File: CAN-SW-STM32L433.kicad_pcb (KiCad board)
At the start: 2 copper layers, 60 x 40 mm, 8 parts, among them U1 STM32L433CCTx

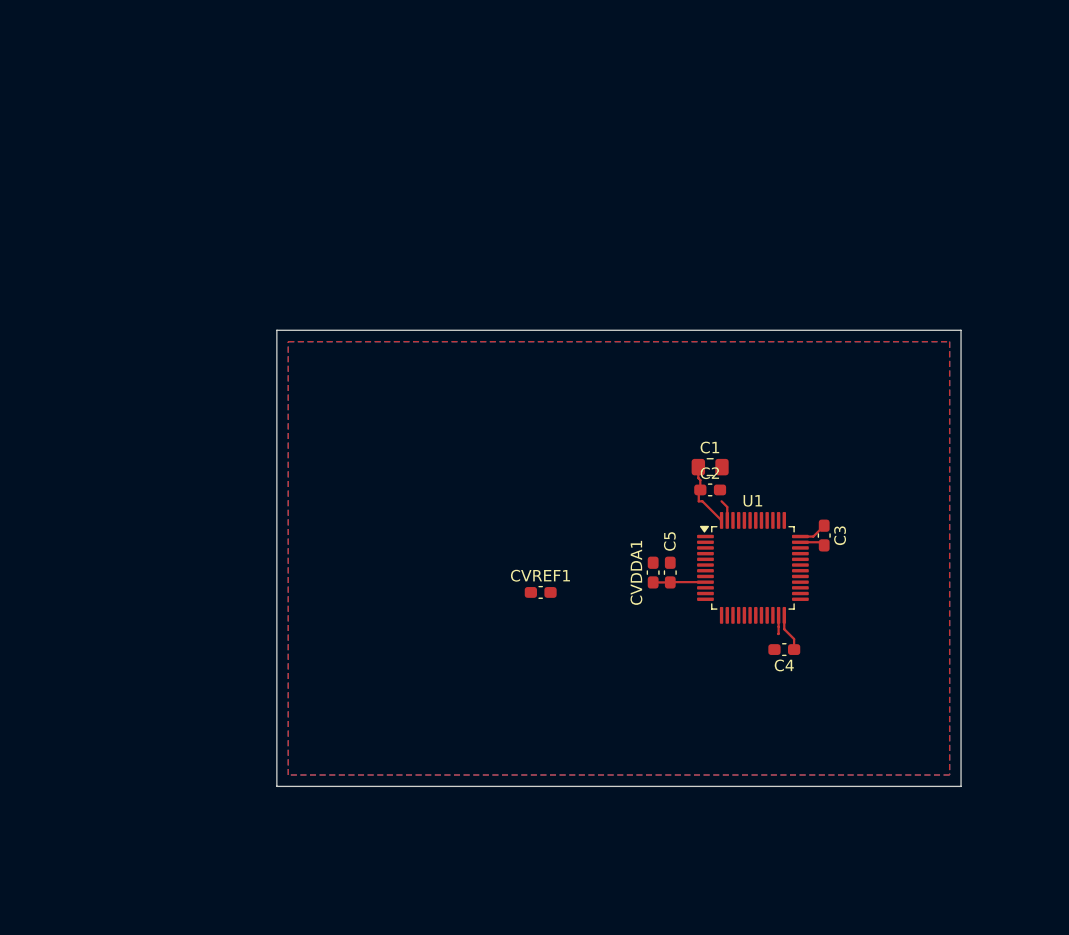
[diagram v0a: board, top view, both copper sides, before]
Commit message: still adding parts, working on basic layout
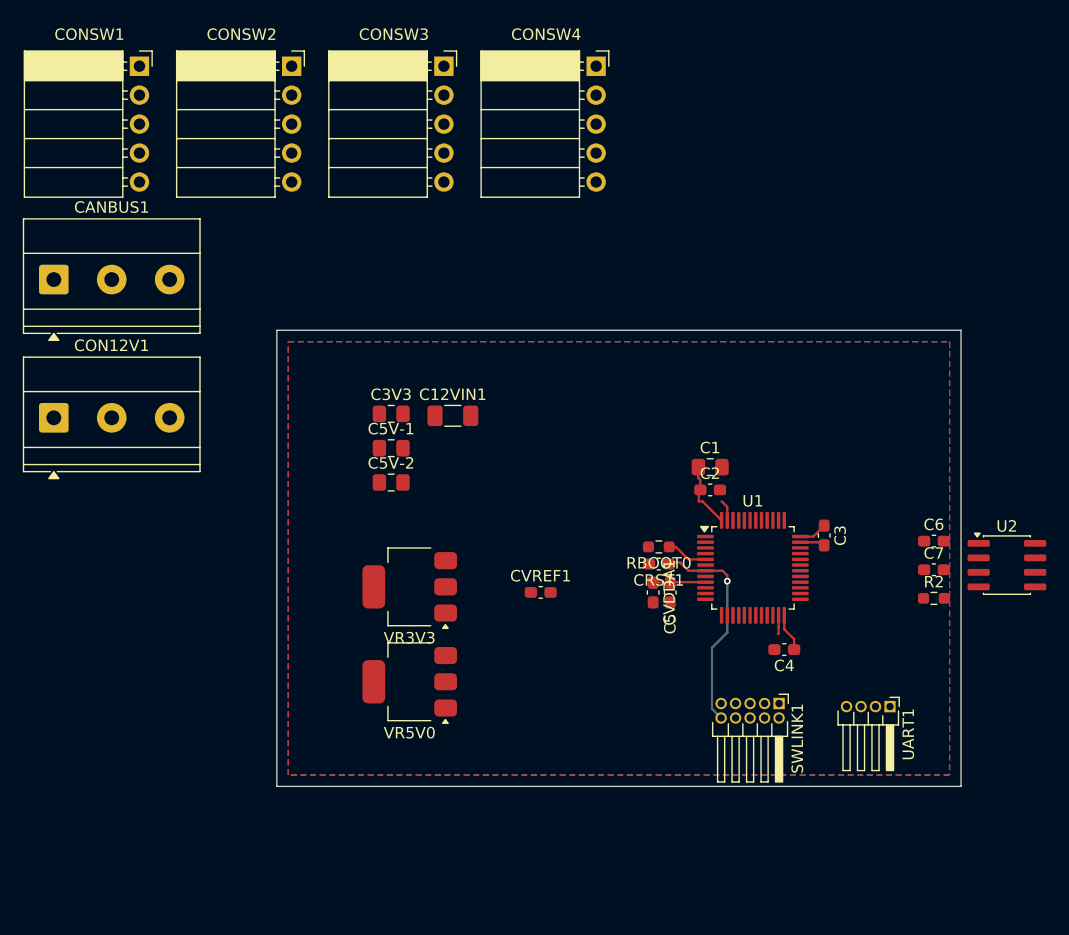
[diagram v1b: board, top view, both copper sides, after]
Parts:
- added C12VIN1: 1u, Capacitor_SMD:C_1206_3216Metric_Pad1.33x1.80mm_HandSolder, F.Cu at (122.4, 85.5)
- added C3V3: 1u, Capacitor_SMD:C_0805_2012Metric_Pad1.18x1.45mm_HandSolder, F.Cu at (117.0, 85.3)
- added C5V-1: 1u, Capacitor_SMD:C_0805_2012Metric_Pad1.18x1.45mm_HandSolder, F.Cu at (117.0, 88.3)
- added C5V-2: 1u, Capacitor_SMD:C_0805_2012Metric_Pad1.18x1.45mm_HandSolder, F.Cu at (117.0, 91.3)
- added C6: 100n, Capacitor_SMD:C_0603_1608Metric_Pad1.08x0.95mm_HandSolder, F.Cu at (164.6, 96.5)
- added C7: 100n, Capacitor_SMD:C_0603_1608Metric_Pad1.08x0.95mm_HandSolder, F.Cu at (164.6, 99.0)
- added CANBUS1: Screw_Terminal_01x03, TerminalBlock_Phoenix:TerminalBlock_Phoenix_MKDS-1,5-3-5.08_1x03_P5.08mm_Horizontal, F.Cu at (87.4, 73.5)
- added CON12V1: CENTER+, TerminalBlock_Phoenix:TerminalBlock_Phoenix_MKDS-1,5-3-5.08_1x03_P5.08mm_Horizontal, F.Cu at (87.4, 85.7)
- added CONSW1: Conn_01x05, Connector_PinSocket_2.54mm:PinSocket_1x05_P2.54mm_Horizontal, F.Cu at (95.0, 54.8)
- added CONSW2: Conn_01x05, Connector_PinSocket_2.54mm:PinSocket_1x05_P2.54mm_Horizontal, F.Cu at (108.3, 54.8)
- added CONSW3: Conn_01x05, Connector_PinSocket_2.54mm:PinSocket_1x05_P2.54mm_Horizontal, F.Cu at (121.7, 54.8)
- added CONSW4: Conn_01x05, Connector_PinSocket_2.54mm:PinSocket_1x05_P2.54mm_Horizontal, F.Cu at (135.0, 54.8)
- added CRST1: 100n, Capacitor_SMD:C_0603_1608Metric_Pad1.08x0.95mm_HandSolder, F.Cu at (140.5, 98.5)
- added R2: 10K, Resistor_SMD:R_0603_1608Metric_Pad0.98x0.95mm_HandSolder, F.Cu at (164.6, 101.5)
- added RBOOT0: 10K, Resistor_SMD:R_0603_1608Metric_Pad0.98x0.95mm_HandSolder, F.Cu at (140.5, 97.0)
- added SWLINK1: Conn_ARM_JTAG_SWD_10, Connector_PinHeader_1.27mm:PinHeader_2x05_P1.27mm_Horizontal, F.Cu at (151.0, 110.7)
- added U2: MCP2562-E-SN, Package_SO:SOIC-8_3.9x4.9mm_P1.27mm, F.Cu at (171.0, 98.6)
- added UART1: Conn_01x04, Connector_PinHeader_1.27mm:PinHeader_1x04_P1.27mm_Horizontal, F.Cu at (160.8, 111.0)
- added VR3V3: TLV1117-33, Package_TO_SOT_SMD:SOT-223-3_TabPin2, F.Cu at (118.7, 100.5)
- added VR5V0: TLV1117-50, Package_TO_SOT_SMD:SOT-223-3_TabPin2, F.Cu at (118.7, 108.8)
- moved C5 1.75 mm to (141.5, 101.0), turned to -90 degrees
- moved CVDDA1 1.75 mm to (140.0, 101.0), turned to -90 degrees
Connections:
- U1 pad 10: unconnected-(U1-PA0-Pad10) -> /ADC1_IN5
- U1 pad 11: unconnected-(U1-PA1-Pad11) -> /ADC1_IN6
- U1 pad 12: unconnected-(U1-PA2-Pad12) -> /ADC1_IN7
- U1 pad 13: unconnected-(U1-PA3-Pad13) -> /ADC1_IN8
- U1 pad 14: unconnected-(U1-PA4-Pad14) -> /ADC1_IN9
- U1 pad 15: unconnected-(U1-PA5-Pad15) -> /ADC1_IN10
- U1 pad 16: unconnected-(U1-PA6-Pad16) -> /ADC1_IN11
- U1 pad 17: unconnected-(U1-PA7-Pad17) -> /ADC1_IN12
- U1 pad 30: unconnected-(U1-PA9-Pad30) -> /USART1_TX
- U1 pad 31: unconnected-(U1-PA10-Pad31) -> /USART1_RX
- U1 pad 34: unconnected-(U1-PA13-Pad34) -> /SWDIO
- U1 pad 37: unconnected-(U1-PA14-Pad37) -> /SWCLK
- U1 pad 39: unconnected-(U1-PB3-Pad39) -> /SWO
- U1 pad 45: unconnected-(U1-PB8-Pad45) -> /CAN1_RX
- U1 pad 46: unconnected-(U1-PB9-Pad46) -> /CAN1_TX
- U1 pad 5: unconnected-(U1-PH0-Pad5) -> /BOOT0
- U1 pad 7: unconnected-(U1-NRST-Pad7) -> /NRST
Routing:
- net /NRST: track 0.00 -> 18.9 mm, vias 0 -> 1
- net /BOOT0: track 0.00 -> 3.63 mm
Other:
- rule pad_to_mask_clearance: 0 -> 0.0508

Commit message: almost done adding parts, working more on layout
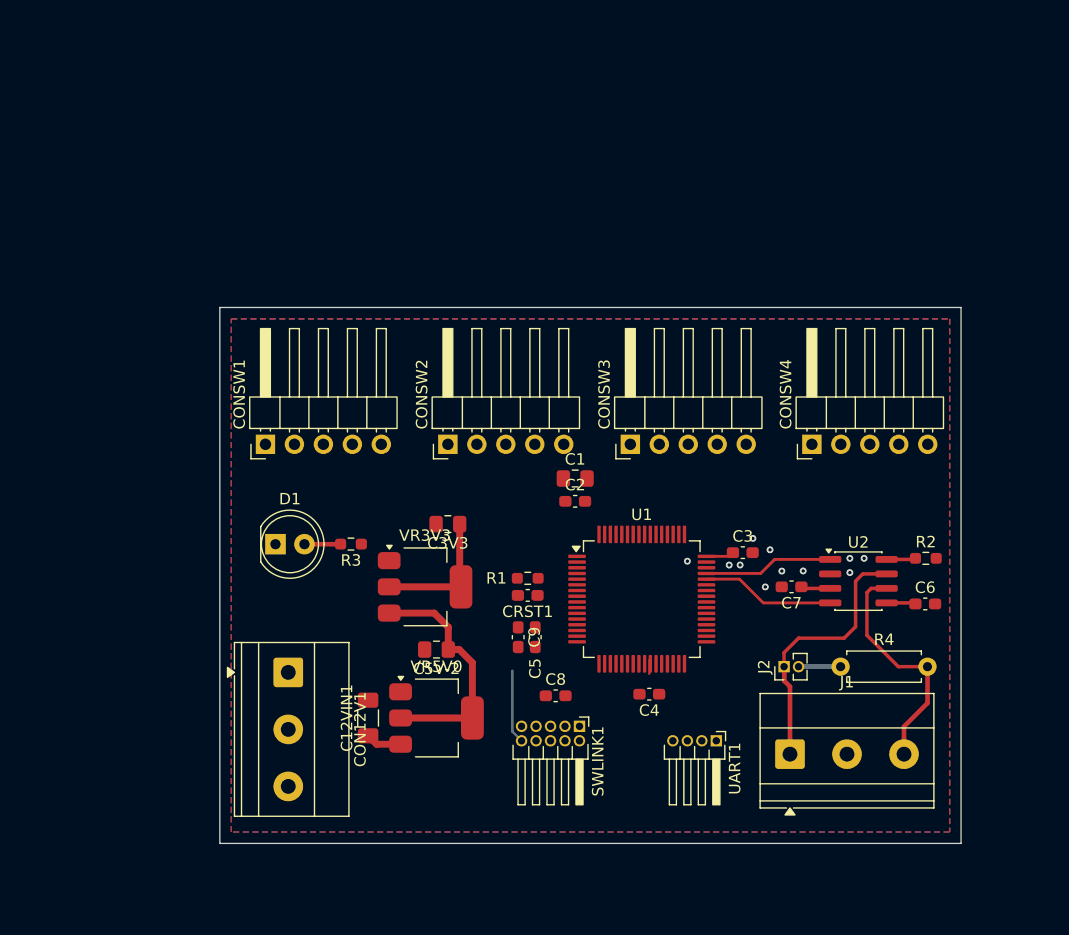
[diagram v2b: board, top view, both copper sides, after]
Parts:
- removed C5V-1: 1u, Capacitor_SMD:C_0805_2012Metric_Pad1.18x1.45mm_HandSolder
- removed CVREF1: 100n, Capacitor_SMD:C_0603_1608Metric_Pad1.08x0.95mm_HandSolder
- added C8: 100n, Capacitor_SMD:C_0603_1608Metric_Pad1.08x0.95mm_HandSolder, F.Cu at (131.4, 110.1)
- added D1: RED, LED_THT:LED_D5.0mm_Clear, F.Cu at (106.9, 96.8)
- added J2: TERM, Connector_PinHeader_1.27mm:PinHeader_1x02_P1.27mm_Vertical, F.Cu at (151.5, 107.5)
- added R3: 1K, Resistor_SMD:R_0603_1608Metric_Pad0.98x0.95mm_HandSolder, F.Cu at (113.5, 96.8)
- added R4: 120R, Resistor_THT:R_Axial_DIN0207_L6.3mm_D2.5mm_P7.62mm_Horizontal, F.Cu at (156.4, 107.5)
- CON12V1: footprint TerminalBlock_Phoenix:TerminalBlock_Phoenix_MKDS-1,5-3-5.08_1x03_P5.08mm_Horizontal -> TerminalBlock_Phoenix:TerminalBlock_Phoenix_MKDS-1,5-3_1x03_P5.00mm_Horizontal
- CONSW1, CONSW2, CONSW3, CONSW4: footprint Connector_PinSocket_2.54mm:PinSocket_1x05_P2.54mm_Horizontal -> Connector_PinHeader_2.54mm:PinHeader_1x05_P2.54mm_Horizontal
- J1: renamed from CANBUS1; value Screw_Terminal_01x03 -> CANBUS; footprint TerminalBlock_Phoenix:TerminalBlock_Phoenix_MKDS-1,5-3-5.08_1x03_P5.08mm_Horizontal -> TerminalBlock_Phoenix:TerminalBlock_Phoenix_MKDS-1,5-3_1x03_P5.00mm_Horizontal
- U1: value STM32L433CCTx -> STM32L433RBTx; footprint Package_QFP:LQFP-48_7x7mm_P0.5mm -> Package_QFP:LQFP-64_10x10mm_P0.5mm
- moved J1 76.8 mm to (152.0, 115.2)
- moved CONSW4 38.2 mm to (153.9, 88.0), turned to 90 degrees
- moved CONSW3 37.0 mm to (138.0, 88.0), turned to 90 degrees
- moved CONSW2 35.9 mm to (122.0, 88.0), turned to 90 degrees
- moved CONSW1 35.0 mm to (106.0, 88.0), turned to 90 degrees
- moved CON12V1 30.3 mm to (108.0, 108.0), turned to -90 degrees
- moved C12VIN1 27.5 mm to (115.0, 112.0), turned to 90 degrees
- moved SWLINK1 17.6 mm to (133.5, 112.7)
- moved UART1 15.5 mm to (145.5, 114.0)
- moved C5V-2 15.2 mm to (121.0, 106.0), turned to 180 degrees
- moved U2 13.1 mm to (158.0, 100.0)
- moved C7 12.6 mm to (152.1, 100.5), turned to 180 degrees
- moved C4 12.5 mm to (139.7, 109.9)
- moved C5 12.5 mm to (129.7, 104.9)
- moved C9 12.5 mm to (128.2, 104.9)
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- renumbered CVDDA1 to C9, RBOOT0 to R1
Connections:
- J1 pad 1: /CANL -> /CANH
- J1 pad 3: /CANH -> /CANL
- U1 pad 10: /ADC1_IN5 -> /ADC1_IN3
- U1 pad 11: /ADC1_IN6 -> /ADC1_IN4
- U1 pad 12: /ADC1_IN7 -> GND
- U1 pad 13: /ADC1_IN8 -> +3.3V
- U1 pad 14: /ADC1_IN9 -> /ADC1_IN5
- U1 pad 15: /ADC1_IN10 -> /ADC1_IN6
- U1 pad 16: /ADC1_IN11 -> /ADC1_IN7
- U1 pad 17: /ADC1_IN12 -> /ADC1_IN8
- U1 pad 18: unconnected-(U1-PB0-Pad18) -> GND
- U1 pad 19: unconnected-(U1-PB1-Pad19) -> +3.3V
- U1 pad 20: unconnected-(U1-PB2-Pad20) -> /ADC1_IN9
- U1 pad 21: unconnected-(U1-PB10-Pad21) -> /ADC1_IN10
- U1 pad 22: unconnected-(U1-PB11-Pad22) -> /ADC1_IN11
- U1 pad 23: GND -> /ADC1_IN12
- U1 pad 24: +3.3V -> unconnected-(U1-PC4-Pad24)
- U1 pad 30: /USART1_TX -> unconnected-(U1-PB11-Pad30)
- U1 pad 31: /USART1_RX -> GND
- U1 pad 32: unconnected-(U1-PA11-Pad32) -> +3.3V
- U1 pad 34: /SWDIO -> unconnected-(U1-PB13-Pad34)
- U1 pad 35: GND -> unconnected-(U1-PB14-Pad35)
- U1 pad 36: +3.3V -> unconnected-(U1-PB15-Pad36)
- U1 pad 37: /SWCLK -> unconnected-(U1-PC6-Pad37)
- U1 pad 39: /SWO -> unconnected-(U1-PC8-Pad39)
- U1 pad 42: unconnected-(U1-PB6-Pad42) -> /USART1_TX
- U1 pad 43: unconnected-(U1-PB7-Pad43) -> /USART1_RX
- U1 pad 44: unconnected-(U1-PH3-Pad44) -> /CAN1_RX
- U1 pad 45: /CAN1_RX -> /CAN1_TX
- U1 pad 46: /CAN1_TX -> /SWDIO
- U1 pad 8: GND -> /ADC1_IN1
- U1 pad 9: +3.3V -> /ADC1_IN2
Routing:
- net +5V: track 0.00 -> 24.0 mm
- net /CANH: track 0.00 -> 23.3 mm
- net /CANL: track 0.00 -> 20.6 mm
- net /NRST: track 18.9 -> 6.49 mm, vias 1 -> 0
- net /CAN1_RX: track 0.00 -> 11.7 mm
- net /CAN1_TX: track 0.00 -> 11.4 mm
- net GND: track 5.74 -> 0.00 mm, vias 0 -> 11
- net Net-(J2-Pin_2): track 0.00 -> 3.69 mm
- net /BOOT0: track 3.63 -> 0.00 mm
- net Net-(D1-A): track 0.00 -> 3.17 mm
- net +12V: track 0.00 -> 3.16 mm
- net Net-(U2-STBY): track 0.00 -> 2.56 mm
- net unconnected-(U1-PB0-Pad26): track 0.00 -> 1.22 mm
- net +3.3V: track 16.3 -> 16.8 mm
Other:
- board size 60 x 40 mm -> 65 x 47 mm

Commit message: more progress on the layout, fixed connector sizes for uart and swlink
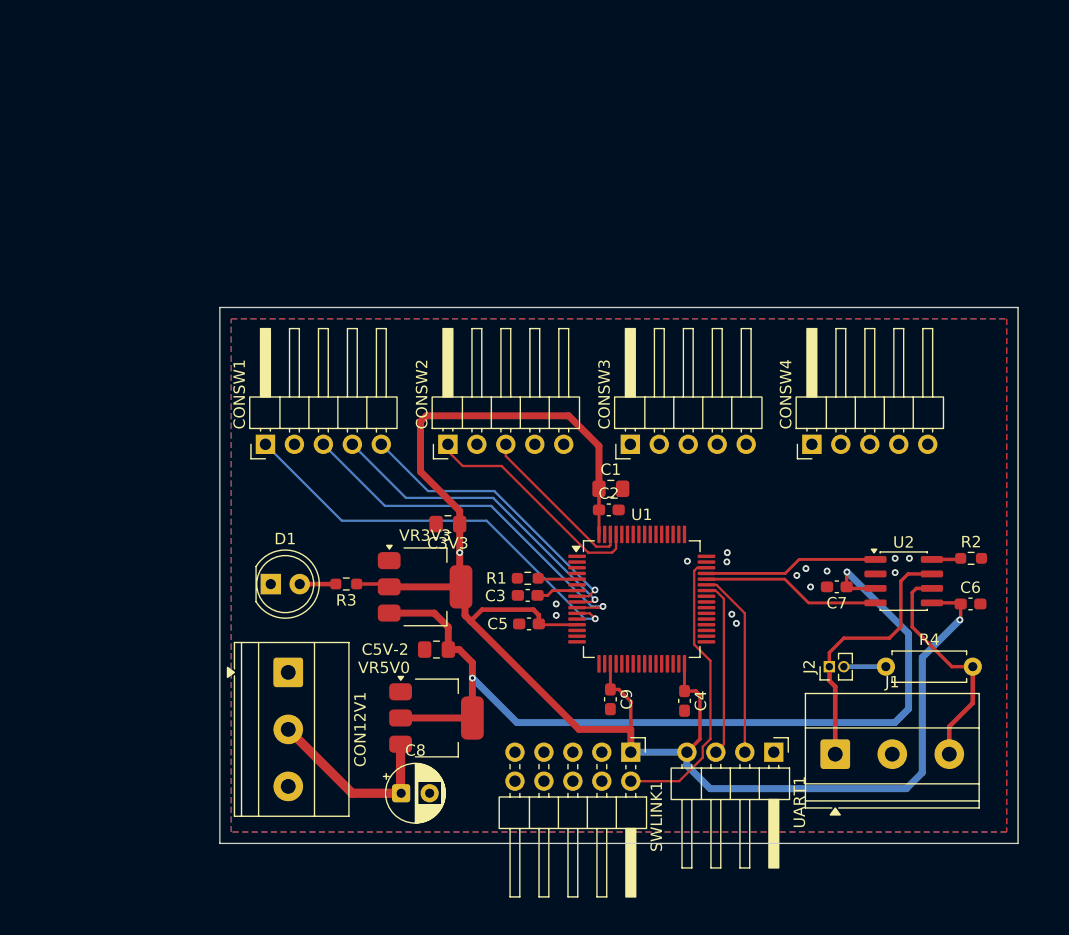
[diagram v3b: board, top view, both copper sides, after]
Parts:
- removed C12VIN1: 1u, Capacitor_SMD:C_1206_3216Metric_Pad1.33x1.80mm_HandSolder
- removed the C3 at (147.9, 97.5)
- C8: value 100n -> 10u; footprint Capacitor_SMD:C_0603_1608Metric_Pad1.08x0.95mm_HandSolder -> Capacitor_THT:CP_Radial_D5.0mm_P2.50mm
- D1: value RED -> 3.3V
- SWLINK1: footprint Connector_PinHeader_1.27mm:PinHeader_2x05_P1.27mm_Horizontal -> Connector_PinHeader_2.54mm:PinHeader_2x05_P2.54mm_Horizontal
- U1: value STM32L433RBTx -> STM32L433RCT3
- UART1: footprint Connector_PinHeader_1.27mm:PinHeader_1x04_P1.27mm_Horizontal -> Connector_PinHeader_2.54mm:PinHeader_1x04_P2.54mm_Horizontal
- moved C8 16.0 mm to (117.9, 118.6)
- moved C9 9.75 mm to (136.2, 110.4)
- moved UART1 5.14 mm to (150.6, 115.0)
- moved SWLINK1 5.04 mm to (138.0, 115.0)
- moved C6 3.97 mm to (167.8, 102.0)
- moved C7 3.97 mm to (156.1, 100.5)
- moved J1 3.97 mm to (156.0, 115.2)
- moved J2 3.97 mm to (155.4, 107.5)
- moved R2 3.97 mm to (167.9, 98.0)
- moved R4 3.97 mm to (160.4, 107.5)
- moved U2 3.97 mm to (162.0, 100.0)
- moved D1 3.52 mm to (106.5, 100.3)
- moved R3 3.52 mm to (113.1, 100.2)
- moved C1 3.25 mm to (136.3, 91.9)
- moved C4 3.14 mm to (142.8, 110.5), turned to -90 degrees
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- renumbered CRST1 to C3
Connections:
- C8 pad 1: +3.3V -> +12V
- CONSW1 pad 4: /IS1 -> /ADC1_IN2
- CONSW1 pad 5: /VS1 -> /ADC1_IN1
- CONSW2 pad 4: /IS2 -> /ADC1_IN4
- CONSW2 pad 5: /VS2 -> /ADC1_IN3
- U1 pad 10: /ADC1_IN3 -> /DEN1
- U1 pad 11: /ADC1_IN4 -> /CTL1
- U1 pad 48: +3.3V -> GND
- U1 pad 61: unconnected-(U1-PB8-Pad61) -> /CTL2
- U1 pad 62: unconnected-(U1-PB9-Pad62) -> /DEN2
- UART1 pad 2: /USART1_TX -> /USART1_RX
- UART1 pad 3: /USART1_RX -> /USART1_TX
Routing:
- net +3.3V: track 16.8 -> 147.1 mm, vias 0 -> 2
- net +5V: track 24.0 -> 79.9 mm, vias 0 -> 2
- net /CTL1: track 0.00 -> 37.1 mm, vias 0 -> 1
- net /DEN1: track 0.00 -> 32.4 mm, vias 0 -> 1
- net /ADC1_IN2: track 0.00 -> 29.1 mm, vias 0 -> 1
- net /ADC1_IN1: track 0.00 -> 25.8 mm, vias 0 -> 1
- net /SWDIO: track 0.00 -> 25.6 mm
- net /CTL2: track 0.00 -> 20.4 mm
- net /USART1_RX: track 0.00 -> 16.6 mm
- net /USART1_TX: track 0.00 -> 15.6 mm
- net /DEN2: track 0.00 -> 14.5 mm
- net +12V: track 3.16 -> 16.5 mm
- net /CAN1_RX: track 11.7 -> 15.7 mm
- net /CAN1_TX: track 11.4 -> 15.3 mm
- net /BOOT0: track 0.00 -> 3.44 mm
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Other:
- board size 65 x 47 mm -> 70 x 47 mm
